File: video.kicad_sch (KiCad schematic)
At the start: 3 parts, among them J2 Board Interconnect Female, J2 Video Output Female

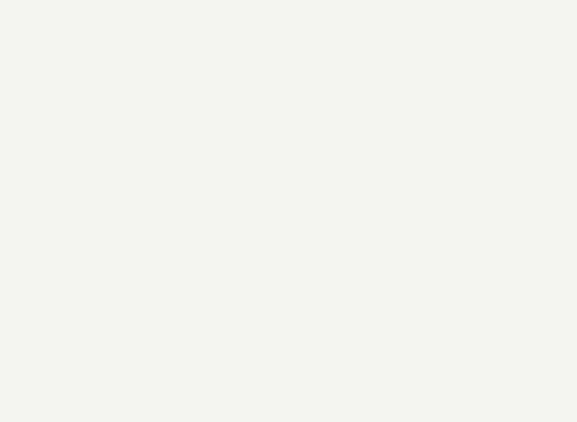
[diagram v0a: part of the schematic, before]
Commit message: complete tracing for fabrication
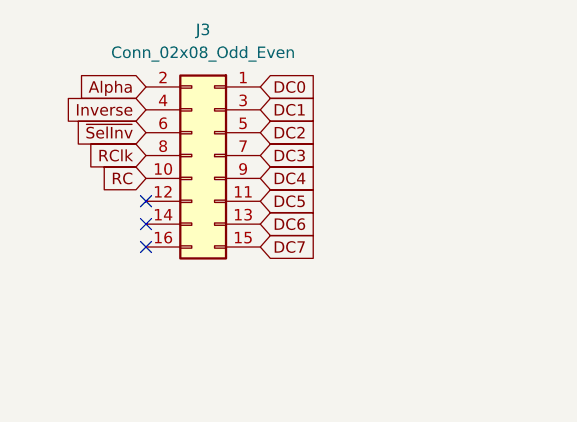
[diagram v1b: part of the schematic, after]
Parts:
- added J3: Conn_02x08_Odd_Even, Connector_PinSocket_2.54mm:PinSocket_2x08_P2.54mm_Vertical, symbol Connector_Generic:Conn_02x08_Odd_Even
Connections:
- new net Alpha: J3.2 (Pin_2)
- new net DC0: J3.1 (Pin_1)
- new net DC1: J3.3 (Pin_3)
- new net DC2: J3.5 (Pin_5)
- new net DC3: J3.7 (Pin_7)
- new net DC4: J3.9 (Pin_9)
- new net DC5: J3.11 (Pin_11)
- new net DC6: J3.13 (Pin_13)
- new net DC7: J3.15 (Pin_15)
- new net Inverse: J3.4 (Pin_4)
- new net RC: J3.10 (Pin_10)
- new net RClk: J3.8 (Pin_8)
- new net ~{SelInv}: J3.6 (Pin_6)
- no-connect marks 2 -> 5
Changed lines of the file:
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@@
   )
   (no_connect (at 167.64 168.91))
+  (no_connect (at 123.19 116.84))
+  (no_connect (at 123.19 121.92))
+  (no_connect (at 123.19 119.38))
   (no_connect (at 124.4092 190.8048))
   (global_label "DO5" (shape input) (at 124.4092 180.6448 180) (fields_autoplaced)
@@
     )
   )
+  (global_label "DC3" (shape input) (at 135.89 111.76 0) (fields_autoplaced)
+    (effects (font (size 1.27 1.27)) (justify left))
+    (property "Intersheetrefs" "${INTERSHEET_REFS}" (at 142.5453 111.76 0)
+      (effects (font (size 1.27 1.27)) (justify left) hide)
+    )
+  )
+  (global_label "DC2" (shape input) (at 135.89 109.22 0) (fields_autoplaced)
+    (effects (font (size 1.27 1.27)) (justify left))
+    (property "Intersheetrefs" "${INTERSHEET_REFS}" (at 142.5453 109.22 0)
+      (effects (font (size 1.27 1.27)) (justify left) hide)
+    )
+  )
+  (global_label "DC7" (shape input) (at 135.89 121.92 0) (fields_autoplaced)
+    (effects (font (size 1.27 1.27)) (justify left))
+    (property "Intersheetrefs" "${INTERSHEET_REFS}" (at 142.5453 121.92 0)
+      (effects (font (size 1.27 1.27)) (justify left) hide)
+    )
+  )
+  (global_label "DC5" (shape input) (at 135.89 116.84 0) (fields_autoplaced)
+    (effects (font (size 1.27 1.27)) (justify left))
+    (property "Intersheetrefs" "${INTERSHEET_REFS}" (at 142.5453 116.84 0)
+      (effects (font (size 1.27 1.27)) (justify left) hide)
+    )
+  )
   (global_label "GM2" (shape input) (at 137.1092 175.5648 0) (fields_autoplaced)
     (effects (font (size 1.27 1.27)) (justify left))
@@
     )
   )
+  (global_label "~{SelInv}" (shape input) (at 123.19 109.22 180) (fields_autoplaced)
+    (effects (font (size 1.27 1.27)) (justify right))
+    (property "Intersheetrefs" "${INTERSHEET_REFS}" (at 114.5201 109.22 0)
+      (effects (font (size 1.27 1.27)) (justify right) hide)
+    )
+  )
   (global_label "~{A}{slash}G" (shape input) (at 137.1092 188.2648 0) (fields_autoplaced)
     (effects (font (size 1.27 1.27)) (justify left))
@@
     )
   )
+  (global_label "DC6" (shape input) (at 135.89 119.38 0) (fields_autoplaced)
+    (effects (font (size 1.27 1.27)) (justify left))
+    (property "Intersheetrefs" "${INTERSHEET_REFS}" (at 142.5453 119.38 0)
+      (effects (font (size 1.27 1.27)) (justify left) hide)
+    )
+  )
   (global_label "CSS" (shape input) (at 124.4092 188.2648 180) (fields_autoplaced)
     (effects (font (size 1.27 1.27)) (justify right))
@@
     )
   )
+  (global_label "RClk" (shape input) (at 123.19 111.76 180) (fields_autoplaced)
+    (effects (font (size 1.27 1.27)) (justify right))
+    (property "Intersheetrefs" "${INTERSHEET_REFS}" (at 116.0509 111.76 0)
+      (effects (font (size 1.27 1.27)) (justify right) hide)
+    )
+  )
+  (global_label "DC0" (shape input) (at 135.89 104.14 0) (fields_autoplaced)
+    (effects (font (size 1.27 1.27)) (justify left))
+    (property "Intersheetrefs" "${INTERSHEET_REFS}" (at 142.5453 104.14 0)
+      (effects (font (size 1.27 1.27)) (justify left) hide)
+    )
+  )
   (global_label "GM0" (shape input) (at 137.1092 180.6448 0) (fields_autoplaced)
     (effects (font (size 1.27 1.27)) (justify left))
@@
     )
   )
+  (global_label "RC" (shape input) (at 123.19 114.3 180) (fields_autoplaced)
+    (effects (font (size 1.27 1.27)) (justify right))
+    (property "Intersheetrefs" "${INTERSHEET_REFS}" (at 117.7442 114.3 0)
+      (effects (font (size 1.27 1.27)) (justify right) hide)
+    )
+  )
   (global_label "VID OUT" (shape output) (at 167.64 171.45 0) (fields_autoplaced)
     (effects (font (size 1.27 1.27)) (justify left))
@@
     )
   )
+  (global_label "DC1" (shape input) (at 135.89 106.68 0) (fields_autoplaced)
+    (effects (font (size 1.27 1.27)) (justify left))
+    (property "Intersheetrefs" "${INTERSHEET_REFS}" (at 142.5453 106.68 0)
+      (effects (font (size 1.27 1.27)) (justify left) hide)
+    )
+  )
+  (global_label "DC4" (shape input) (at 135.89 114.3 0) (fields_autoplaced)
+    (effects (font (size 1.27 1.27)) (justify left))
+    (property "Intersheetrefs" "${INTERSHEET_REFS}" (at 142.5453 114.3 0)
+      (effects (font (size 1.27 1.27)) (justify left) hide)
+    )
+  )
   (global_label "~{RAS0}" (shape input) (at 137.1092 183.1848 0) (fields_autoplaced)
     (effects (font (size 1.27 1.27)) (justify left))
@@
     (effects (font (size 1.27 1.27)) (justify right))
     (property "Intersheetrefs" "${INTERSHEET_REFS}" (at 118.3476 170.4848 0)
+      (effects (font (size 1.27 1.27)) (justify right) hide)
+    )
+  )
+  (global_label "Inverse" (shape input) (at 123.19 106.68 180) (fields_autoplaced)
+    (effects (font (size 1.27 1.27)) (justify right))
+    (property "Intersheetrefs" "${INTERSHEET_REFS}" (at 113.4919 106.68 0)
+      (effects (font (size 1.27 1.27)) (justify right) hide)
+    )
+  )
+  (global_label "Alpha" (shape input) (at 123.19 104.14 180) (fields_autoplaced)
+    (effects (font (size 1.27 1.27)) (justify right))
+    (property "Intersheetrefs" "${INTERSHEET_REFS}" (at 115.004 104.14 0)
       (effects (font (size 1.27 1.27)) (justify right) hide)
     )
@@
         )
       )
+    )
+  )
+  (symbol (lib_id "Connector_Generic:Conn_02x08_Odd_Even") (at 130.81 111.76 0) (mirror y) (unit 1)
+    (in_bom yes) (on_board yes) (dnp no)
+    (property "Reference" "J3" (at 129.54 97.79 0)
+      (effects (font (size 1.27 1.27)))
+    )
+    (property "Value" "Conn_02x08_Odd_Even" (at 129.54 100.33 0)
+      (effects (font (size 1.27 1.27)))
+    )
+    (property "Footprint" "Connector_PinSocket_2.54mm:PinSocket_2x08_P2.54mm_Vertical" (at 130.81 111.76 0)
+      (effects (font (size 1.27 1.27)) hide)
+    )
+    (property "Datasheet" "~" (at 130.81 111.76 0)
+      (effects (font (size 1.27 1.27)) hide)
+    )
+    (pin "1")
+    (pin "10")
+    (pin "11")
+    (pin "12")
+    (pin "13")
+    (pin "14")
+    (pin "15")
+    (pin "16")
+    (pin "2")
+    (pin "3")
+    (pin "4")
+    (pin "5")
+    (pin "6")
+    (pin "7")
+    (pin "8")
+    (pin "9")
+    (instances
+      (project "Dragon32"
+        (path "/0c3dceba-7c95-4b3d-b590-0eb581444beb/d9dba8db-e731-4cb4-b2de-fefd65b288bc"
+          (reference "J3") (unit 1)
+        )
+      )
+      (project "extrom"
+        (path "/cb53a310-2b71-496c-b1c6-02a74c835e55/8385a6af-0c63-454e-b740-6be48e6405de"
+          (reference "J3") (unit 1)
+        )
+      )

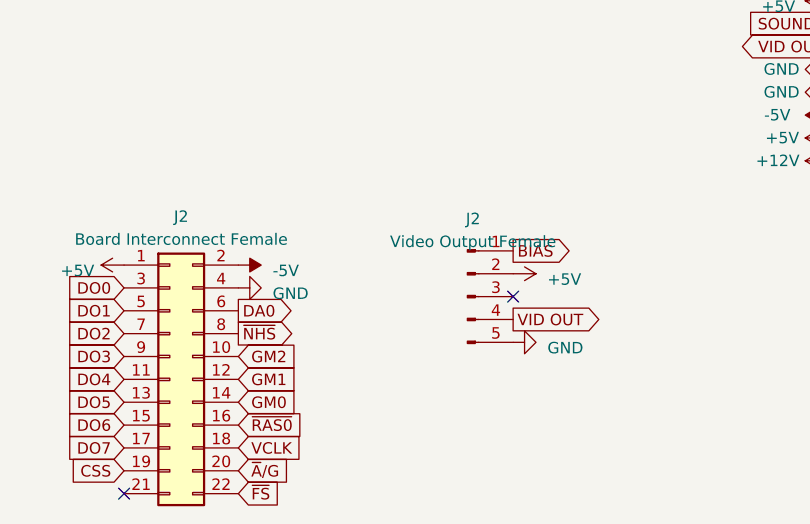
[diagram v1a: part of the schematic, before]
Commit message: move -5v
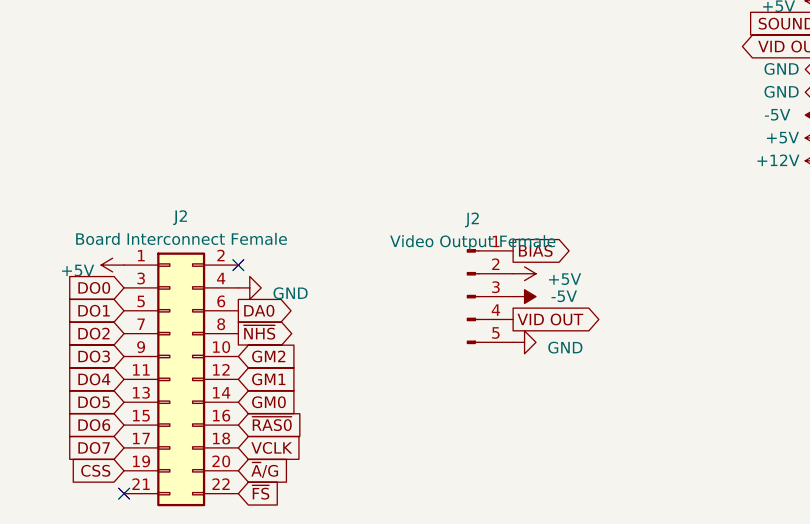
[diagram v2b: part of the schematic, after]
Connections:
- net -5V: now also J2.3 (Pin_3); no longer J2.2 (Pin_2)
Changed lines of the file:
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@@
     (comment 2 "Reposition dram and buffer")
   )
-  (no_connect (at 167.64 168.91))
   (no_connect (at 123.19 116.84))
   (no_connect (at 123.19 121.92))
   (no_connect (at 123.19 119.38))
+  (no_connect (at 137.1092 165.4048))
   (no_connect (at 124.4092 190.8048))
   (global_label "DO5" (shape input) (at 124.4092 180.6448 180) (fields_autoplaced)
@@
     )
   )
-  (symbol (lib_id "power:-5V") (at 137.1092 165.4048 270) (unit 1)
-    (in_bom yes) (on_board yes) (dnp no) (fields_autoplaced)
-    (property "Reference" "#PWR064" (at 139.6492 165.4048 0)
-      (effects (font (size 1.27 1.27)) hide)
-    )
-    (property "Value" "-5V" (at 140.9192 166.0398 90)
-      (effects (font (size 1.27 1.27)) (justify left))
-    )
-    (property "Footprint" "" (at 137.1092 165.4048 0)
-      (effects (font (size 1.27 1.27)) hide)
-    )
-    (property "Datasheet" "" (at 137.1092 165.4048 0)
-      (effects (font (size 1.27 1.27)) hide)
-    )
-    (pin "1")
-    (instances
-      (project "Dragon32"
-        (path "/0c3dceba-7c95-4b3d-b590-0eb581444beb"
-          (reference "#PWR064") (unit 1)
-        )
-        (path "/0c3dceba-7c95-4b3d-b590-0eb581444beb/d9dba8db-e731-4cb4-b2de-fefd65b288bc"
-          (reference "#PWR06") (unit 1)
-        )
-      )
-      (project "DragonNTSC"
-        (path "/5c3ccdac-dbfc-47b7-be5c-593b42d2b61c"
-          (reference "#PWR04") (unit 1)
-        )
-      )
-    )
-  )
   (symbol (lib_id "Connector_Generic:Conn_02x08_Odd_Even") (at 130.81 111.76 0) (mirror y) (unit 1)
     (in_bom yes) (on_board yes) (dnp no)
@@
         )
       )
+    )
+  )
+  (symbol (lib_id "power:-5V") (at 167.64 168.91 270) (unit 1)
+    (in_bom yes) (on_board yes) (dnp no)
+    (property "Reference" "#PWR048" (at 170.18 168.91 0)
+      (effects (font (size 1.27 1.27)) hide)
+    )
+    (property "Value" "-5V" (at 174.752 168.91 90)
+      (effects (font (size 1.27 1.27)) (justify right))
+    )
+    (property "Footprint" "" (at 167.64 168.91 0)
+      (effects (font (size 1.27 1.27)) hide)
+    )
+    (property "Datasheet" "" (at 167.64 168.91 0)
+      (effects (font (size 1.27 1.27)) hide)
+    )
+    (pin "1")
+    (instances
+      (project "Dragon32"
+        (path "/0c3dceba-7c95-4b3d-b590-0eb581444beb/d9dba8db-e731-4cb4-b2de-fefd65b288bc"
+          (reference "#PWR048") (unit 1)
+        )
+      )
